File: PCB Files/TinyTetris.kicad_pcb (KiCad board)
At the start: 2 copper layers, 40 x 57 mm, 14 parts, among them SW5 SW_SPDT, U1 ATTINY85-20PU

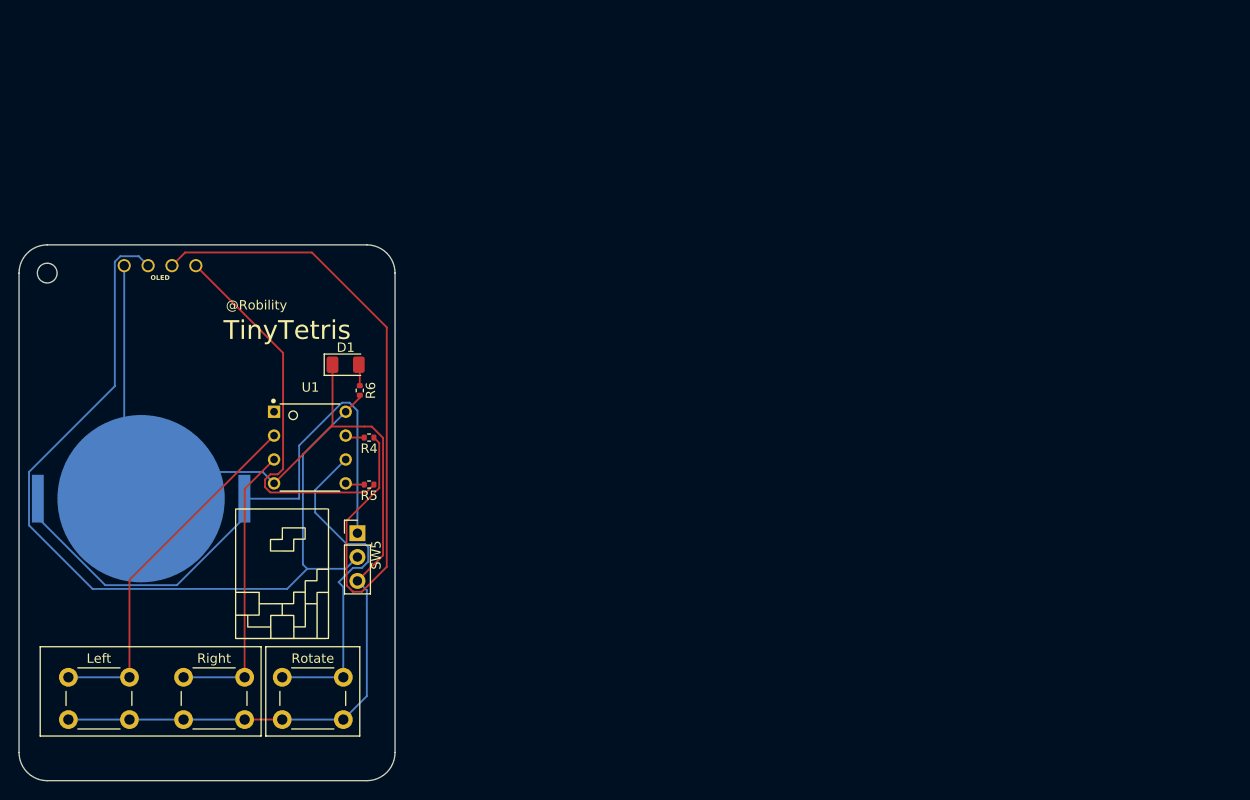
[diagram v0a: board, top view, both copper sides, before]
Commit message: Update PCB Files
The PCB is thinner, the power LED was removed, and the power switch is a different type
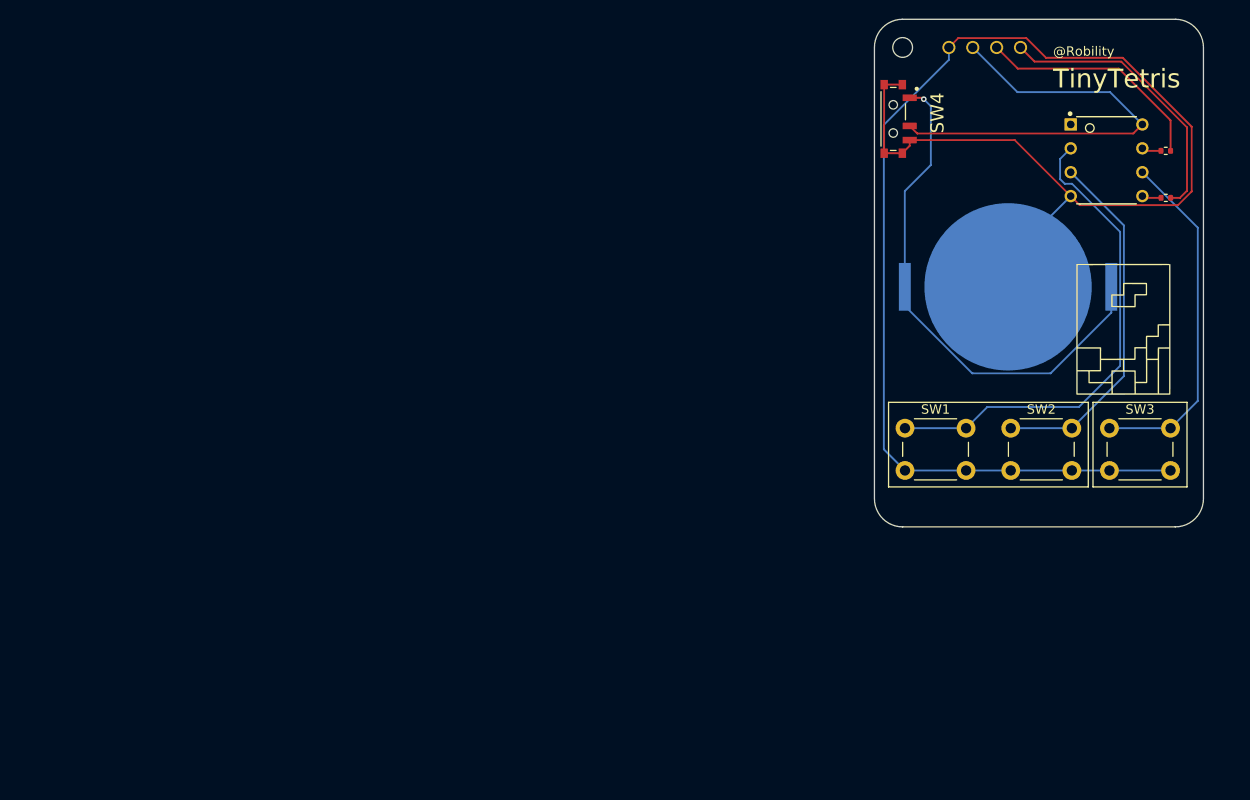
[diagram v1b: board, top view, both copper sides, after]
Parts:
- removed D1: LED, LED_SMD:LED_1206_3216Metric
- removed the G*** at (147.0, 89.0)
- removed R6: 470, Resistor_SMD:R_0402_1005Metric
- removed SW5: SW_SPDT, Connector_PinHeader_2.54mm:PinHeader_1x03_P2.54mm_Vertical
- added SW4: PCM12SMTR, footprints:SW_PCM12SMTR, F.Cu at (212.0, 40.6)
- moved BT1 94.9 mm to (224.2, 58.5)
- moved REF** 94.1 mm to (213.0, 33.0)
- moved G*** 93.2 mm to (236.5, 63.0)
- moved SW1 92.9 mm to (213.2, 73.5)
- moved SW2 91.9 mm to (224.5, 73.5)
- moved SW3 91.9 mm to (235.0, 73.5)
- moved OL1 90.7 mm to (221.7, 33.0)
- moved U1 90.1 mm to (234.7, 45.0)
- moved R5 90.1 mm to (241.0, 49.0)
- moved R4 90.1 mm to (241.0, 44.0)
- renumbered Left to SW1, Right to SW2, Rotate to SW3
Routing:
- net SCL: track 75.3 -> 25.0 mm
- net VCC: track 96.3 -> 46.9 mm
- net GND: track 124.4 -> 172.9 mm
- net Left: track 38.6 -> 52.3 mm
- net SDA: track 40.8 -> 30.0 mm
- net VBUS: track 64.9 -> 55.4 mm, vias 0 -> 1
- net Right: track 31.0 -> 38.4 mm
- net Net-(D1-A): track 2.27 -> 0.00 mm
- net Rotate: track 36.6 -> 37.4 mm
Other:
- board size 40 x 57 mm -> 35 x 54 mm
